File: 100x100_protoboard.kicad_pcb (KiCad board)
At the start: 2 copper layers, 97.8 x 96.5 mm, 418 parts, among them CON1 BARREL_JACK, CON2 USB_FEMALE_WITH_ID, CON3 USB_FEMALE_WITH_ID, J1 INTERCONNECT_1X03, J10 INTERCONNECT_1X03, J11 INTERCONNECT_1X03, J12 INTERCONNECT_1X03, J13 INTERCONNECT_1X03, J14 INTERCONNECT_1X03, J15 INTERCONNECT_1X03, J16 INTERCONNECT_1X03, J17 INTERCONNECT_1X03, J18 INTERCONNECT_1X03, J19 INTERCONNECT_1X03, J2 INTERCONNECT_1X03, J20 INTERCONNECT_1X03, J21 INTERCONNECT_1X03, J22 INTERCONNECT_1X03, J23 INTERCONNECT_1X03, J24 INTERCONNECT_1X03, J25 INTERCONNECT_1X03, J26 INTERCONNECT_1X03, J27 INTERCONNECT_1X03, J28 INTERCONNECT_1X03, J29 INTERCONNECT_1X03, J3 INTERCONNECT_1X03, J30 INTERCONNECT_1X03, J31 INTERCONNECT_1X03, J32 INTERCONNECT_1X03, J33 INTERCONNECT_1X03, J34 INTERCONNECT_1X03, J35 INTERCONNECT_1X03, J36 INTERCONNECT_1X03, J37 INTERCONNECT_1X03, J38 INTERCONNECT_1X03, J39 INTERCONNECT_1X03, J4 INTERCONNECT_1X03, J40 INTERCONNECT_1X03, J41 INTERCONNECT_1X03, J42 INTERCONNECT_1X03, J43 INTERCONNECT_1X03, J44 INTERCONNECT_1X03, J45 INTERCONNECT_1X03, J46 INTERCONNECT_1X03, J47 INTERCONNECT_1X03, J48 INTERCONNECT_1X03, J49 INTERCONNECT_1X03, J5 INTERCONNECT_1X03, J50 INTERCONNECT_1X03, J51 INTERCONNECT_1X03, J52 INTERCONNECT_1X03, J53 INTERCONNECT_1X03, J54 INTERCONNECT_1X03, J55 INTERCONNECT_1X03, J56 INTERCONNECT_1X03, J57 INTERCONNECT_1X03, J58 INTERCONNECT_1X03, J59 INTERCONNECT_1X03, J6 INTERCONNECT_1X03, J60 INTERCONNECT_1X03, J61 INTERCONNECT_1X03, J62 INTERCONNECT_1X03, J63 INTERCONNECT_1X03, J64 INTERCONNECT_1X03, J65 INTERCONNECT_1X02, J7 INTERCONNECT_1X03, J8 INTERCONNECT_1X03, J9 INTERCONNECT_1X03, P1 CONN_5, P1 CONN_8X2, P2 CONN_8X2, U1 LM7805CT

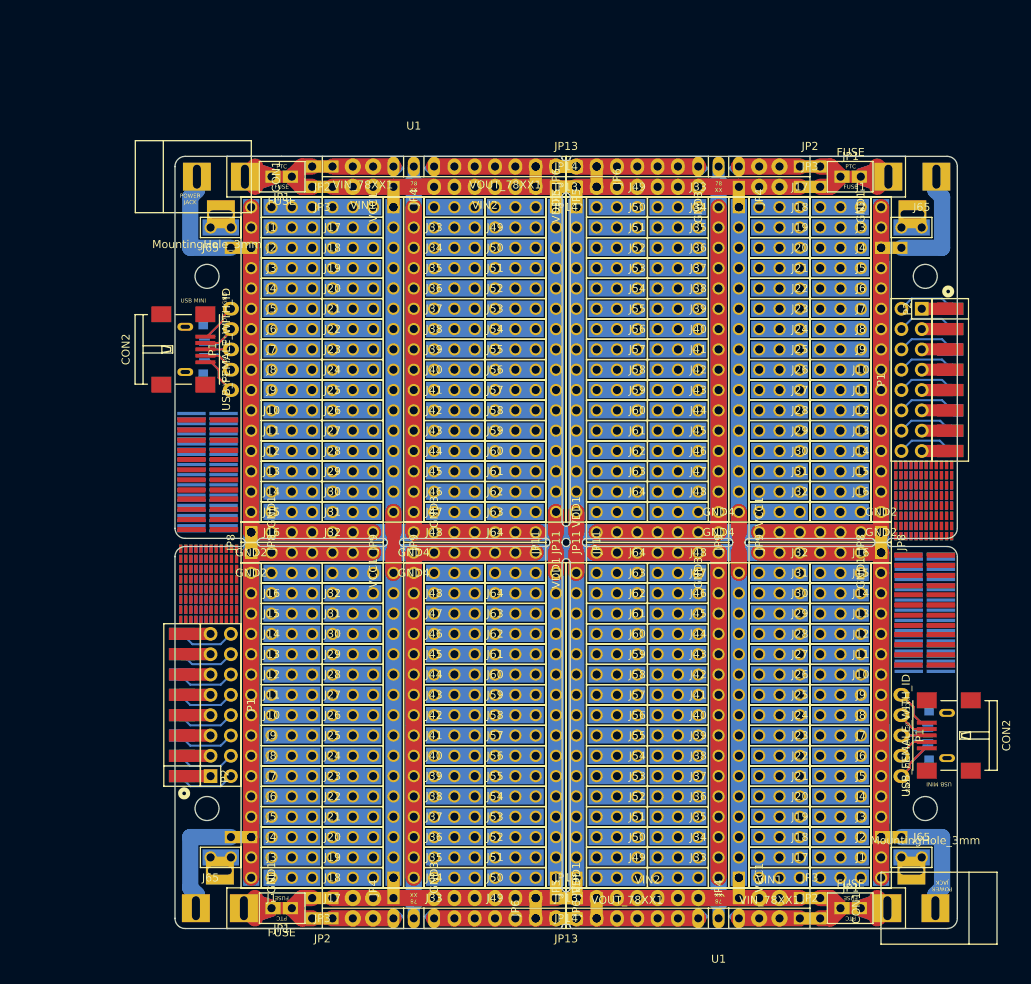
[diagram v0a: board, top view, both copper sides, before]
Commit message: added 3*3 mouse bites between the sub-boards on both edges
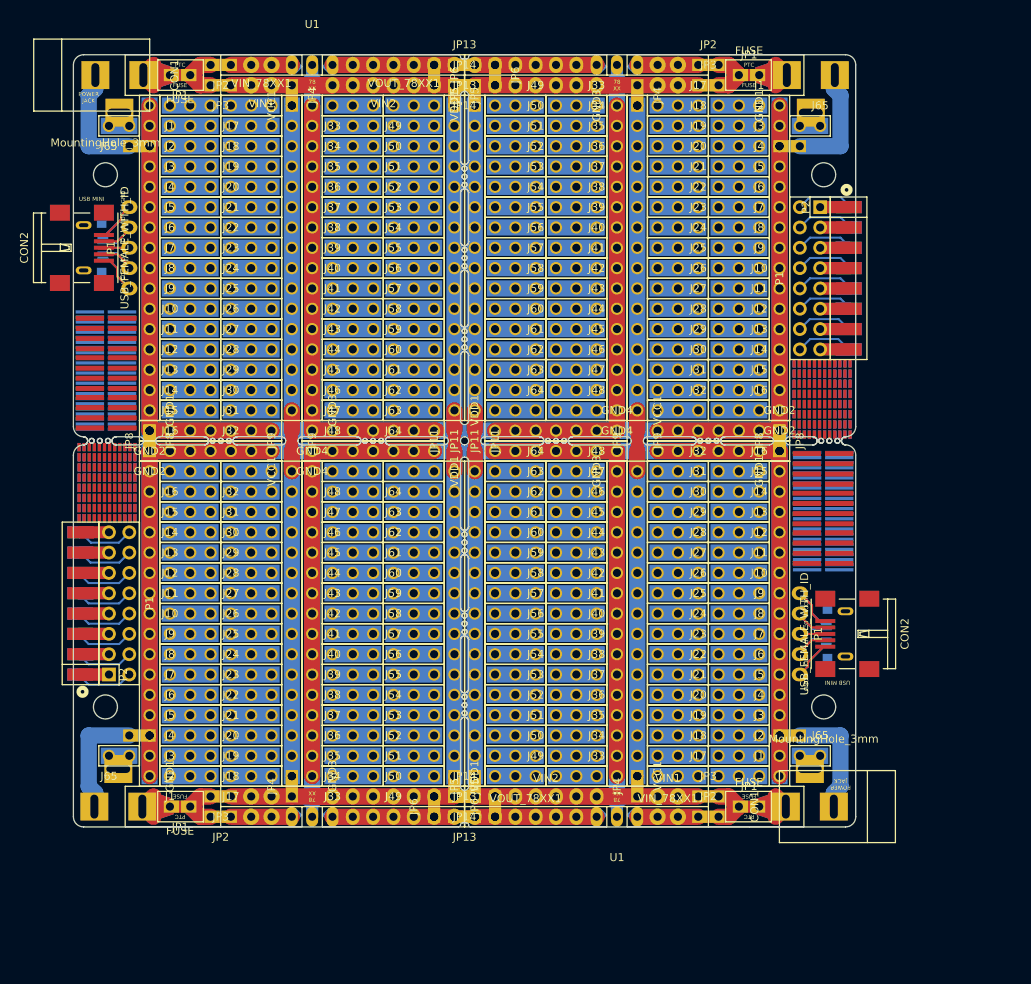
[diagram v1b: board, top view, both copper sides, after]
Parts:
- removed the C1 at (106.7, 35.3)
- removed the C1 at (106.7, 127.3)
- removed the C2 at (104.1, 35.3)
- removed the C2 at (104.1, 127.3)
- removed the CON1 at (132.8, 35.6)
- removed the CON1 at (132.7, 127.0)
- removed the F1 at (121.9, 35.6)
- removed the F1 at (121.9, 127.0)
- removed the F2 at (121.9, 35.6)
- removed the F2 at (121.9, 127.0)
- removed the GND1 at (125.7, 39.4)
- removed the GND1 at (125.7, 85.1)
- removed the GND2 at (125.7, 80.0)
- removed the GND2 at (125.7, 82.5)
- removed the GND3 at (105.4, 39.4)
- removed the GND3 at (105.4, 85.1)
- removed the GND4 at (105.4, 80.0)
- removed the GND4 at (105.4, 82.5)
- removed the J1 at (123.2, 39.4)
- removed the J1 at (123.2, 123.2)
- removed the J10 at (123.2, 62.2)
- removed the J10 at (123.2, 100.3)
- removed the J11 at (123.2, 64.8)
- removed the J11 at (123.2, 97.8)
- removed the J12 at (123.2, 67.3)
- removed the J12 at (123.2, 95.2)
- removed the J13 at (123.2, 69.8)
- removed the J13 at (123.2, 92.7)
- removed the J14 at (123.2, 72.4)
- removed the J14 at (123.2, 90.2)
- removed the J15 at (123.2, 74.9)
- removed the J15 at (123.2, 87.6)
- removed the J16 at (123.2, 77.5)
- removed the J16 at (123.2, 85.1)
- removed the J17 at (115.6, 39.4)
- removed the J17 at (115.6, 123.2)
- removed the J18 at (115.6, 41.9)
- removed the J18 at (115.6, 120.7)
- removed the J19 at (115.6, 44.5)
- removed the J19 at (115.6, 118.1)
- removed the J2 at (123.2, 41.9)
- removed the J2 at (123.2, 120.7)
- removed the J20 at (115.6, 47.0)
- removed the J20 at (115.6, 115.6)
- removed the J21 at (115.6, 49.5)
- removed the J21 at (115.6, 113.0)
- removed the J22 at (115.6, 52.1)
- removed the J22 at (115.6, 110.5)
- removed the J23 at (115.6, 54.6)
- removed the J23 at (115.6, 108.0)
- removed the J24 at (115.6, 57.1)
- removed the J24 at (115.6, 105.4)
- removed the J25 at (115.6, 59.7)
- removed the J25 at (115.6, 102.9)
- removed the J26 at (115.6, 62.2)
- removed the J26 at (115.6, 100.3)
- removed the J27 at (115.6, 64.8)
- removed the J27 at (115.6, 97.8)
- removed the J28 at (115.6, 67.3)
- removed the J28 at (115.6, 95.2)
- removed the J29 at (115.6, 69.8)
- removed the J29 at (115.6, 92.7)
- removed the J3 at (123.2, 44.5)
- removed the J3 at (123.2, 118.1)
- removed the J30 at (115.6, 72.4)
- removed the J30 at (115.6, 90.2)
- removed the J31 at (115.6, 74.9)
- removed the J31 at (115.6, 87.6)
- removed the J32 at (115.6, 77.5)
- removed the J32 at (115.6, 85.1)
- removed the J33 at (102.9, 39.4)
- removed the J33 at (102.9, 123.2)
- removed the J34 at (102.9, 41.9)
- removed the J34 at (102.9, 120.7)
- removed the J35 at (102.9, 44.5)
- removed the J35 at (102.9, 118.1)
- removed the J36 at (102.9, 47.0)
- removed the J36 at (102.9, 115.6)
- removed the J37 at (102.9, 49.5)
- removed the J37 at (102.9, 113.0)
- removed the J38 at (102.9, 52.1)
- removed the J38 at (102.9, 110.5)
- removed the J39 at (102.9, 54.6)
- removed the J39 at (102.9, 108.0)
- removed the J4 at (123.2, 47.0)
- removed the J4 at (123.2, 115.6)
- removed the J40 at (102.9, 57.1)
- removed the J40 at (102.9, 105.4)
- removed the J41 at (102.9, 59.7)
- removed the J41 at (102.9, 102.9)
- removed the J42 at (102.9, 62.2)
- removed the J42 at (102.9, 100.3)
- removed the J43 at (102.9, 64.8)
- removed the J43 at (102.9, 97.8)
- removed the J44 at (102.9, 67.3)
- removed the J44 at (102.9, 95.2)
- removed the J45 at (102.9, 69.8)
- removed the J45 at (102.9, 92.7)
- removed the J46 at (102.9, 72.4)
- removed the J46 at (102.9, 90.2)
- removed the J47 at (102.9, 74.9)
- removed the J47 at (102.9, 87.6)
- removed the J48 at (102.9, 77.5)
- removed the J48 at (102.9, 85.1)
- removed the J49 at (95.2, 39.4)
- removed the J49 at (95.2, 123.2)
- removed the J5 at (123.2, 49.5)
- removed the J5 at (123.2, 113.0)
- removed the J50 at (95.2, 41.9)
- removed the J50 at (95.2, 120.7)
- removed the J51 at (95.2, 44.5)
- removed the J51 at (95.2, 118.1)
- removed the J52 at (95.2, 47.0)
- removed the J52 at (95.2, 115.6)
- removed the J53 at (95.2, 49.5)
- removed the J53 at (95.2, 113.0)
- removed the J54 at (95.2, 52.1)
- removed the J54 at (95.2, 110.5)
- removed the J55 at (95.2, 54.6)
- removed the J55 at (95.2, 108.0)
- removed the J56 at (95.2, 57.1)
- removed the J56 at (95.2, 105.4)
- removed the J57 at (95.2, 59.7)
- removed the J57 at (95.2, 102.9)
- removed the J58 at (95.2, 62.2)
- removed the J58 at (95.2, 100.3)
- removed the J59 at (95.2, 64.8)
- removed the J59 at (95.2, 97.8)
- removed the J6 at (123.2, 52.1)
- removed the J6 at (123.2, 110.5)
- removed the J60 at (95.2, 67.3)
- removed the J60 at (95.2, 95.2)
- removed the J61 at (95.2, 69.8)
- removed the J61 at (95.2, 92.7)
- removed the J62 at (95.2, 72.4)
- removed the J62 at (95.2, 90.2)
- removed the J63 at (95.2, 74.9)
- removed the J63 at (95.2, 87.6)
- removed the J64 at (95.2, 77.5)
- removed the J64 at (95.2, 85.1)
- removed the J65 at (130.8, 41.9)
- removed the J65 at (130.8, 120.7)
- removed the J7 at (123.2, 54.6)
- removed the J7 at (123.2, 108.0)
- removed the J8 at (123.2, 57.1)
- removed the J8 at (123.2, 105.4)
- removed the J9 at (123.2, 59.7)
- removed the J9 at (123.2, 102.9)
- removed the JP1 at (121.9, 35.6)
- removed the JP1 at (121.9, 127.0)
- removed the JP10 at (87.6, 81.3) (x2)
- removed the JP11 at (87.6, 81.3) (x2)
- removed the JP12 at (86.4, 80.0)
- removed the JP12 at (86.4, 82.5)
- removed the JP13 at (86.4, 34.3)
- removed the JP13 at (86.4, 128.3)
- removed the JP14 at (86.4, 36.8)
- removed the JP14 at (86.4, 125.7)
- removed the JP15 at (108.0, 81.3) (x2)
- removed the JP2 at (116.8, 34.3)
- removed the JP2 at (116.8, 128.3)
- removed the JP3 at (116.8, 36.8)
- removed the JP3 at (116.8, 125.7)
- removed the JP4 at (108.0, 38.1)
- removed the JP4 at (108.0, 124.5)
- removed the JP5 at (87.6, 38.1)
- removed the JP5 at (87.6, 124.5)
- removed the JP6 at (90.2, 35.6)
- removed the JP6 at (90.2, 127.0)
- removed the JP7 at (127.0, 44.5)
- removed the JP7 at (127.0, 118.1)
- removed the JP8 at (125.7, 81.3) (x2)
- removed the JP9 at (108.0, 81.3) (x2)
- removed the MountingHole_3mm at (131.2, 48.0)
- removed the MountingHole_3mm at (131.2, 114.5)
- removed the P1 at (129.5, 61.0)
- removed the P1 at (128.3, 105.4)
- removed the Ref** at (131.7, 78.6) (x2)
- removed the Ref** at (131.2, 95.2)
- removed the Ref** at (131.7, 73.5) (x2)
- removed the Ref** at (131.2, 94.7)
- removed the Ref** at (131.2, 89.7)
- removed the Ref** at (131.2, 84.8)
- removed the Ref** at (131.2, 85.0)
- removed the Ref** at (131.2, 90.1)
- removed the U1 at (105.4, 34.3)
- removed the U1 at (105.4, 128.3)
- removed the VCC1 at (108.0, 77.5)
- removed the VCC1 at (108.0, 123.2)
- removed the VDD1 at (87.6, 39.4)
- removed the VDD1 at (87.6, 85.1)
- removed the VIN1 at (111.8, 36.8)
- removed the VIN1 at (111.8, 125.7)
- removed the VIN2 at (96.5, 36.8)
- removed the VIN2 at (96.5, 125.7)
- removed the VIN_78XX1 at (111.8, 34.3)
- removed the VIN_78XX1 at (111.8, 128.3)
- removed the VOUT_78XX1 at (94.0, 34.3)
- removed the VOUT_78XX1 at (94.0, 128.3)
- added C1: u33, Capacitors_SMD:C_0805_HandSoldering, B.Cu at (94.0, 22.6)
- added C1: u33, Capacitors_SMD:C_0805_HandSoldering, B.Cu at (94.0, 114.6)
- added C2: u1, Capacitors_SMD:C_0805_HandSoldering, B.Cu at (91.4, 22.6)
- added C2: u1, Capacitors_SMD:C_0805_HandSoldering, B.Cu at (91.4, 114.6)
- added CON1: BARREL_JACK, Connect:BARREL_JACK, B.Cu at (120.1, 22.9)
- added CON1: BARREL_JACK, Connect:BARREL_JACK, F.Cu at (120.0, 114.3)
- added F1: FUSE, Muonde:CC12ZZ, B.Cu at (109.2, 22.9)
- added F1: FUSE, Muonde:CC12ZZ, F.Cu at (109.2, 114.3)
- added F2: FUSE, Muonde:CC12ZZ, F.Cu at (109.2, 22.9)
- added F2: FUSE, Muonde:CC12ZZ, B.Cu at (109.2, 114.3)
- added GND1: INTERCONNECT_1X16, 2.54mm_Pin_Headers:Interconnect_1x16, F.Cu at (113.0, 26.7)
- added GND1: INTERCONNECT_1X16, 2.54mm_Pin_Headers:Interconnect_1x16, F.Cu at (113.0, 72.4)
- added GND2: INTERCONNECT_1X07, 2.54mm_Pin_Headers:Interconnect_1x07, F.Cu at (113.0, 67.3)
- added GND2: INTERCONNECT_1X07, 2.54mm_Pin_Headers:Interconnect_1x07, F.Cu at (113.0, 69.8)
- added GND3: INTERCONNECT_1X16, 2.54mm_Pin_Headers:Interconnect_1x16, F.Cu at (92.7, 26.7)
- added GND3: INTERCONNECT_1X16, 2.54mm_Pin_Headers:Interconnect_1x16, F.Cu at (92.7, 72.4)
- added GND4: INTERCONNECT_1X07, 2.54mm_Pin_Headers:Interconnect_1x07, F.Cu at (92.7, 67.3)
- added GND4: INTERCONNECT_1X07, 2.54mm_Pin_Headers:Interconnect_1x07, F.Cu at (92.7, 69.8)
- added J1: INTERCONNECT_1X03, 2.54mm_Pin_Headers:Interconnect_1x03, F.Cu at (110.5, 26.7)
- added J1: INTERCONNECT_1X03, 2.54mm_Pin_Headers:Interconnect_1x03, F.Cu at (110.5, 110.5)
- added J10: INTERCONNECT_1X03, 2.54mm_Pin_Headers:Interconnect_1x03, F.Cu at (110.5, 49.5)
- added J10: INTERCONNECT_1X03, 2.54mm_Pin_Headers:Interconnect_1x03, F.Cu at (110.5, 87.6)
- added J11: INTERCONNECT_1X03, 2.54mm_Pin_Headers:Interconnect_1x03, F.Cu at (110.5, 52.1)
- added J11: INTERCONNECT_1X03, 2.54mm_Pin_Headers:Interconnect_1x03, F.Cu at (110.5, 85.1)
- added J12: INTERCONNECT_1X03, 2.54mm_Pin_Headers:Interconnect_1x03, F.Cu at (110.5, 54.6)
- added J12: INTERCONNECT_1X03, 2.54mm_Pin_Headers:Interconnect_1x03, F.Cu at (110.5, 82.5)
- added J13: INTERCONNECT_1X03, 2.54mm_Pin_Headers:Interconnect_1x03, F.Cu at (110.5, 57.1)
- added J13: INTERCONNECT_1X03, 2.54mm_Pin_Headers:Interconnect_1x03, F.Cu at (110.5, 80.0)
- added J14: INTERCONNECT_1X03, 2.54mm_Pin_Headers:Interconnect_1x03, F.Cu at (110.5, 59.7)
- added J14: INTERCONNECT_1X03, 2.54mm_Pin_Headers:Interconnect_1x03, F.Cu at (110.5, 77.5)
- added J15: INTERCONNECT_1X03, 2.54mm_Pin_Headers:Interconnect_1x03, F.Cu at (110.5, 62.2)
- added J15: INTERCONNECT_1X03, 2.54mm_Pin_Headers:Interconnect_1x03, F.Cu at (110.5, 74.9)
- added J16: INTERCONNECT_1X03, 2.54mm_Pin_Headers:Interconnect_1x03, F.Cu at (110.5, 64.8)
- added J16: INTERCONNECT_1X03, 2.54mm_Pin_Headers:Interconnect_1x03, F.Cu at (110.5, 72.4)
- added J17: INTERCONNECT_1X03, 2.54mm_Pin_Headers:Interconnect_1x03, F.Cu at (102.9, 26.7)
- added J17: INTERCONNECT_1X03, 2.54mm_Pin_Headers:Interconnect_1x03, F.Cu at (102.9, 110.5)
- added J18: INTERCONNECT_1X03, 2.54mm_Pin_Headers:Interconnect_1x03, F.Cu at (102.9, 29.2)
- added J18: INTERCONNECT_1X03, 2.54mm_Pin_Headers:Interconnect_1x03, F.Cu at (102.9, 108.0)
- added J19: INTERCONNECT_1X03, 2.54mm_Pin_Headers:Interconnect_1x03, F.Cu at (102.9, 31.8)
- added J19: INTERCONNECT_1X03, 2.54mm_Pin_Headers:Interconnect_1x03, F.Cu at (102.9, 105.4)
- added J2: INTERCONNECT_1X03, 2.54mm_Pin_Headers:Interconnect_1x03, F.Cu at (110.5, 29.2)
- added J2: INTERCONNECT_1X03, 2.54mm_Pin_Headers:Interconnect_1x03, F.Cu at (110.5, 108.0)
- added J20: INTERCONNECT_1X03, 2.54mm_Pin_Headers:Interconnect_1x03, F.Cu at (102.9, 34.3)
- added J20: INTERCONNECT_1X03, 2.54mm_Pin_Headers:Interconnect_1x03, F.Cu at (102.9, 102.9)
- added J21: INTERCONNECT_1X03, 2.54mm_Pin_Headers:Interconnect_1x03, F.Cu at (102.9, 36.8)
- added J21: INTERCONNECT_1X03, 2.54mm_Pin_Headers:Interconnect_1x03, F.Cu at (102.9, 100.3)
- added J22: INTERCONNECT_1X03, 2.54mm_Pin_Headers:Interconnect_1x03, F.Cu at (102.9, 39.4)
- added J22: INTERCONNECT_1X03, 2.54mm_Pin_Headers:Interconnect_1x03, F.Cu at (102.9, 97.8)
- added J23: INTERCONNECT_1X03, 2.54mm_Pin_Headers:Interconnect_1x03, F.Cu at (102.9, 41.9)
- added J23: INTERCONNECT_1X03, 2.54mm_Pin_Headers:Interconnect_1x03, F.Cu at (102.9, 95.2)
- added J24: INTERCONNECT_1X03, 2.54mm_Pin_Headers:Interconnect_1x03, F.Cu at (102.9, 44.5)
- added J24: INTERCONNECT_1X03, 2.54mm_Pin_Headers:Interconnect_1x03, F.Cu at (102.9, 92.7)
- added J25: INTERCONNECT_1X03, 2.54mm_Pin_Headers:Interconnect_1x03, F.Cu at (102.9, 47.0)
- added J25: INTERCONNECT_1X03, 2.54mm_Pin_Headers:Interconnect_1x03, F.Cu at (102.9, 90.2)
- added J26: INTERCONNECT_1X03, 2.54mm_Pin_Headers:Interconnect_1x03, F.Cu at (102.9, 49.5)
- added J26: INTERCONNECT_1X03, 2.54mm_Pin_Headers:Interconnect_1x03, F.Cu at (102.9, 87.6)
- added J27: INTERCONNECT_1X03, 2.54mm_Pin_Headers:Interconnect_1x03, F.Cu at (102.9, 52.1)
- added J27: INTERCONNECT_1X03, 2.54mm_Pin_Headers:Interconnect_1x03, F.Cu at (102.9, 85.1)
- added J28: INTERCONNECT_1X03, 2.54mm_Pin_Headers:Interconnect_1x03, F.Cu at (102.9, 54.6)
- added J28: INTERCONNECT_1X03, 2.54mm_Pin_Headers:Interconnect_1x03, F.Cu at (102.9, 82.5)
- added J29: INTERCONNECT_1X03, 2.54mm_Pin_Headers:Interconnect_1x03, F.Cu at (102.9, 57.1)
- added J29: INTERCONNECT_1X03, 2.54mm_Pin_Headers:Interconnect_1x03, F.Cu at (102.9, 80.0)
- added J3: INTERCONNECT_1X03, 2.54mm_Pin_Headers:Interconnect_1x03, F.Cu at (110.5, 31.8)
- added J3: INTERCONNECT_1X03, 2.54mm_Pin_Headers:Interconnect_1x03, F.Cu at (110.5, 105.4)
- added J30: INTERCONNECT_1X03, 2.54mm_Pin_Headers:Interconnect_1x03, F.Cu at (102.9, 59.7)
- added J30: INTERCONNECT_1X03, 2.54mm_Pin_Headers:Interconnect_1x03, F.Cu at (102.9, 77.5)
- added J31: INTERCONNECT_1X03, 2.54mm_Pin_Headers:Interconnect_1x03, F.Cu at (102.9, 62.2)
- added J31: INTERCONNECT_1X03, 2.54mm_Pin_Headers:Interconnect_1x03, F.Cu at (102.9, 74.9)
- added J32: INTERCONNECT_1X03, 2.54mm_Pin_Headers:Interconnect_1x03, F.Cu at (102.9, 64.8)
- added J32: INTERCONNECT_1X03, 2.54mm_Pin_Headers:Interconnect_1x03, F.Cu at (102.9, 72.4)
- added J33: INTERCONNECT_1X03, 2.54mm_Pin_Headers:Interconnect_1x03, F.Cu at (90.2, 26.7)
- added J33: INTERCONNECT_1X03, 2.54mm_Pin_Headers:Interconnect_1x03, F.Cu at (90.2, 110.5)
- added J34: INTERCONNECT_1X03, 2.54mm_Pin_Headers:Interconnect_1x03, F.Cu at (90.2, 29.2)
- added J34: INTERCONNECT_1X03, 2.54mm_Pin_Headers:Interconnect_1x03, F.Cu at (90.2, 108.0)
- added J35: INTERCONNECT_1X03, 2.54mm_Pin_Headers:Interconnect_1x03, F.Cu at (90.2, 31.8)
- added J35: INTERCONNECT_1X03, 2.54mm_Pin_Headers:Interconnect_1x03, F.Cu at (90.2, 105.4)
- added J36: INTERCONNECT_1X03, 2.54mm_Pin_Headers:Interconnect_1x03, F.Cu at (90.2, 34.3)
- added J36: INTERCONNECT_1X03, 2.54mm_Pin_Headers:Interconnect_1x03, F.Cu at (90.2, 102.9)
- added J37: INTERCONNECT_1X03, 2.54mm_Pin_Headers:Interconnect_1x03, F.Cu at (90.2, 36.8)
- added J37: INTERCONNECT_1X03, 2.54mm_Pin_Headers:Interconnect_1x03, F.Cu at (90.2, 100.3)
- added J38: INTERCONNECT_1X03, 2.54mm_Pin_Headers:Interconnect_1x03, F.Cu at (90.2, 39.4)
- added J38: INTERCONNECT_1X03, 2.54mm_Pin_Headers:Interconnect_1x03, F.Cu at (90.2, 97.8)
- added J39: INTERCONNECT_1X03, 2.54mm_Pin_Headers:Interconnect_1x03, F.Cu at (90.2, 41.9)
- added J39: INTERCONNECT_1X03, 2.54mm_Pin_Headers:Interconnect_1x03, F.Cu at (90.2, 95.2)
- added J4: INTERCONNECT_1X03, 2.54mm_Pin_Headers:Interconnect_1x03, F.Cu at (110.5, 34.3)
- added J4: INTERCONNECT_1X03, 2.54mm_Pin_Headers:Interconnect_1x03, F.Cu at (110.5, 102.9)
- added J40: INTERCONNECT_1X03, 2.54mm_Pin_Headers:Interconnect_1x03, F.Cu at (90.2, 44.5)
- added J40: INTERCONNECT_1X03, 2.54mm_Pin_Headers:Interconnect_1x03, F.Cu at (90.2, 92.7)
- added J41: INTERCONNECT_1X03, 2.54mm_Pin_Headers:Interconnect_1x03, F.Cu at (90.2, 47.0)
- added J41: INTERCONNECT_1X03, 2.54mm_Pin_Headers:Interconnect_1x03, F.Cu at (90.2, 90.2)
- added J42: INTERCONNECT_1X03, 2.54mm_Pin_Headers:Interconnect_1x03, F.Cu at (90.2, 49.5)
- added J42: INTERCONNECT_1X03, 2.54mm_Pin_Headers:Interconnect_1x03, F.Cu at (90.2, 87.6)
- added J43: INTERCONNECT_1X03, 2.54mm_Pin_Headers:Interconnect_1x03, F.Cu at (90.2, 52.1)
- added J43: INTERCONNECT_1X03, 2.54mm_Pin_Headers:Interconnect_1x03, F.Cu at (90.2, 85.1)
- added J44: INTERCONNECT_1X03, 2.54mm_Pin_Headers:Interconnect_1x03, F.Cu at (90.2, 54.6)
- added J44: INTERCONNECT_1X03, 2.54mm_Pin_Headers:Interconnect_1x03, F.Cu at (90.2, 82.5)
- added J45: INTERCONNECT_1X03, 2.54mm_Pin_Headers:Interconnect_1x03, F.Cu at (90.2, 57.1)
- added J45: INTERCONNECT_1X03, 2.54mm_Pin_Headers:Interconnect_1x03, F.Cu at (90.2, 80.0)
- added J46: INTERCONNECT_1X03, 2.54mm_Pin_Headers:Interconnect_1x03, F.Cu at (90.2, 59.7)
- added J46: INTERCONNECT_1X03, 2.54mm_Pin_Headers:Interconnect_1x03, F.Cu at (90.2, 77.5)
- added J47: INTERCONNECT_1X03, 2.54mm_Pin_Headers:Interconnect_1x03, F.Cu at (90.2, 62.2)
- added J47: INTERCONNECT_1X03, 2.54mm_Pin_Headers:Interconnect_1x03, F.Cu at (90.2, 74.9)
- added J48: INTERCONNECT_1X03, 2.54mm_Pin_Headers:Interconnect_1x03, F.Cu at (90.2, 64.8)
- added J48: INTERCONNECT_1X03, 2.54mm_Pin_Headers:Interconnect_1x03, F.Cu at (90.2, 72.4)
- added J49: INTERCONNECT_1X03, 2.54mm_Pin_Headers:Interconnect_1x03, F.Cu at (82.5, 26.7)
- added J49: INTERCONNECT_1X03, 2.54mm_Pin_Headers:Interconnect_1x03, F.Cu at (82.5, 110.5)
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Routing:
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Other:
- outline, holes or cut-outs redrawn

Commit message: Revert "added 3*3 mouse bites between the sub-boards on both edges"
This reverts commit 72bb31031476af87d888838294cc72f0395ed406.

it turns out that mouse bites shorts the rails if the board house does
not adhere to the NPTH drill directions, which kind of makes up for the
usefulness that the mouse bites provided. and they did not improve the
board sturdiness significantly, so it is not a problem to remove them.
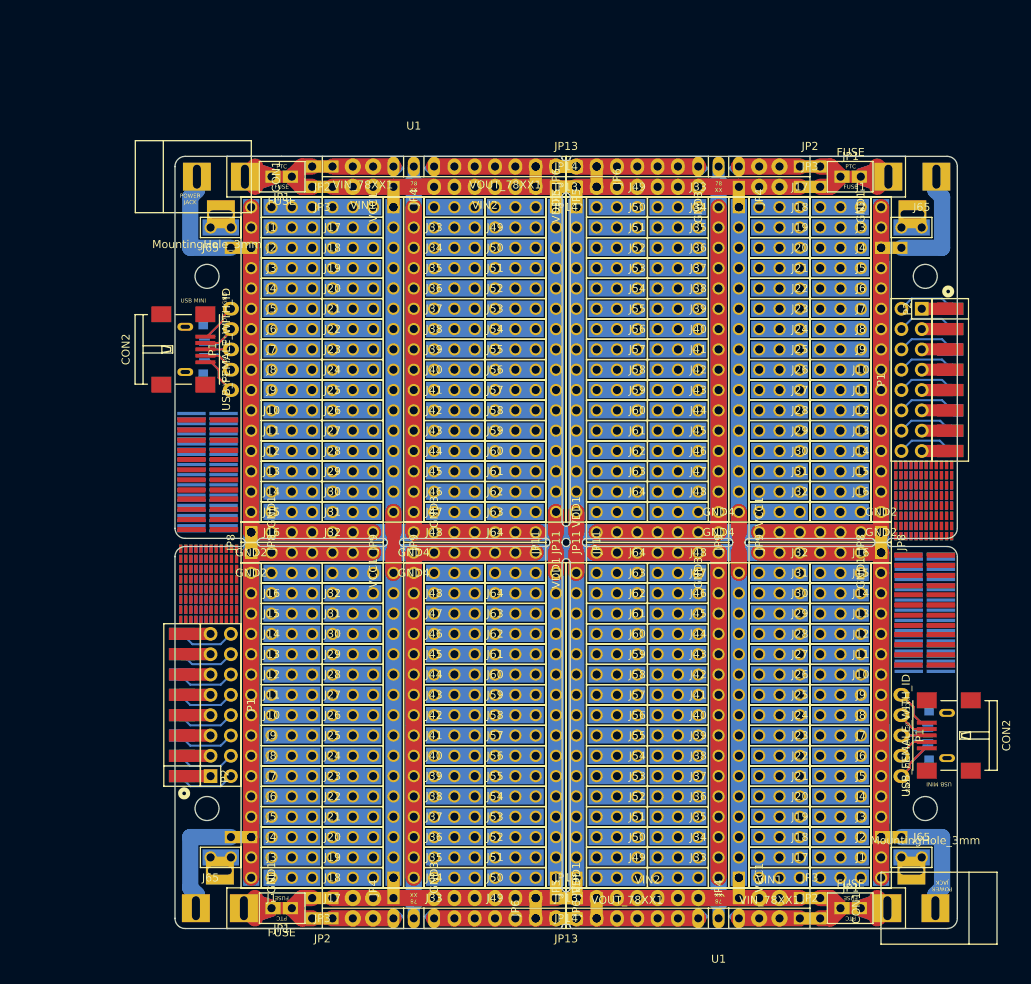
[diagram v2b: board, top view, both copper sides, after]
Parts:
- removed the C1 at (94.0, 22.6)
- removed the C1 at (94.0, 114.6)
- removed the C2 at (91.4, 22.6)
- removed the C2 at (91.4, 114.6)
- removed the CON1 at (120.1, 22.9)
- removed the CON1 at (120.0, 114.3)
- removed the F1 at (109.2, 22.9)
- removed the F1 at (109.2, 114.3)
- removed the F2 at (109.2, 22.9)
- removed the F2 at (109.2, 114.3)
- removed the GND1 at (113.0, 26.7)
- removed the GND1 at (113.0, 72.4)
- removed the GND2 at (113.0, 67.3)
- removed the GND2 at (113.0, 69.8)
- removed the GND3 at (92.7, 26.7)
- removed the GND3 at (92.7, 72.4)
- removed the GND4 at (92.7, 67.3)
- removed the GND4 at (92.7, 69.8)
- removed the J1 at (110.5, 26.7)
- removed the J1 at (110.5, 110.5)
- removed the J10 at (110.5, 49.5)
- removed the J10 at (110.5, 87.6)
- removed the J11 at (110.5, 52.1)
- removed the J11 at (110.5, 85.1)
- removed the J12 at (110.5, 54.6)
- removed the J12 at (110.5, 82.5)
- removed the J13 at (110.5, 57.1)
- removed the J13 at (110.5, 80.0)
- removed the J14 at (110.5, 59.7)
- removed the J14 at (110.5, 77.5)
- removed the J15 at (110.5, 62.2)
- removed the J15 at (110.5, 74.9)
- removed the J16 at (110.5, 64.8)
- removed the J16 at (110.5, 72.4)
- removed the J17 at (102.9, 26.7)
- removed the J17 at (102.9, 110.5)
- removed the J18 at (102.9, 29.2)
- removed the J18 at (102.9, 108.0)
- removed the J19 at (102.9, 31.8)
- removed the J19 at (102.9, 105.4)
- removed the J2 at (110.5, 29.2)
- removed the J2 at (110.5, 108.0)
- removed the J20 at (102.9, 34.3)
- removed the J20 at (102.9, 102.9)
- removed the J21 at (102.9, 36.8)
- removed the J21 at (102.9, 100.3)
- removed the J22 at (102.9, 39.4)
- removed the J22 at (102.9, 97.8)
- removed the J23 at (102.9, 41.9)
- removed the J23 at (102.9, 95.2)
- removed the J24 at (102.9, 44.5)
- removed the J24 at (102.9, 92.7)
- removed the J25 at (102.9, 47.0)
- removed the J25 at (102.9, 90.2)
- removed the J26 at (102.9, 49.5)
- removed the J26 at (102.9, 87.6)
- removed the J27 at (102.9, 52.1)
- removed the J27 at (102.9, 85.1)
- removed the J28 at (102.9, 54.6)
- removed the J28 at (102.9, 82.5)
- removed the J29 at (102.9, 57.1)
- removed the J29 at (102.9, 80.0)
- removed the J3 at (110.5, 31.8)
- removed the J3 at (110.5, 105.4)
- removed the J30 at (102.9, 59.7)
- removed the J30 at (102.9, 77.5)
- removed the J31 at (102.9, 62.2)
- removed the J31 at (102.9, 74.9)
- removed the J32 at (102.9, 64.8)
- removed the J32 at (102.9, 72.4)
- removed the J33 at (90.2, 26.7)
- removed the J33 at (90.2, 110.5)
- removed the J34 at (90.2, 29.2)
- removed the J34 at (90.2, 108.0)
- removed the J35 at (90.2, 31.8)
- removed the J35 at (90.2, 105.4)
- removed the J36 at (90.2, 34.3)
- removed the J36 at (90.2, 102.9)
- removed the J37 at (90.2, 36.8)
- removed the J37 at (90.2, 100.3)
- removed the J38 at (90.2, 39.4)
- removed the J38 at (90.2, 97.8)
- removed the J39 at (90.2, 41.9)
- removed the J39 at (90.2, 95.2)
- removed the J4 at (110.5, 34.3)
- removed the J4 at (110.5, 102.9)
- removed the J40 at (90.2, 44.5)
- removed the J40 at (90.2, 92.7)
- removed the J41 at (90.2, 47.0)
- removed the J41 at (90.2, 90.2)
- removed the J42 at (90.2, 49.5)
- removed the J42 at (90.2, 87.6)
- removed the J43 at (90.2, 52.1)
- removed the J43 at (90.2, 85.1)
- removed the J44 at (90.2, 54.6)
- removed the J44 at (90.2, 82.5)
- removed the J45 at (90.2, 57.1)
- removed the J45 at (90.2, 80.0)
- removed the J46 at (90.2, 59.7)
- removed the J46 at (90.2, 77.5)
- removed the J47 at (90.2, 62.2)
- removed the J47 at (90.2, 74.9)
- removed the J48 at (90.2, 64.8)
- removed the J48 at (90.2, 72.4)
- removed the J49 at (82.5, 26.7)
- removed the J49 at (82.5, 110.5)
- removed the J5 at (110.5, 36.8)
- removed the J5 at (110.5, 100.3)
- removed the J50 at (82.5, 29.2)
- removed the J50 at (82.5, 108.0)
- removed the J51 at (82.5, 31.8)
- removed the J51 at (82.5, 105.4)
- removed the J52 at (82.5, 34.3)
- removed the J52 at (82.5, 102.9)
- removed the J53 at (82.5, 36.8)
- removed the J53 at (82.5, 100.3)
- removed the J54 at (82.5, 39.4)
- removed the J54 at (82.5, 97.8)
- removed the J55 at (82.5, 41.9)
- removed the J55 at (82.5, 95.2)
- removed the J56 at (82.5, 44.5)
- removed the J56 at (82.5, 92.7)
- removed the J57 at (82.5, 47.0)
- removed the J57 at (82.5, 90.2)
- removed the J58 at (82.5, 49.5)
- removed the J58 at (82.5, 87.6)
- removed the J59 at (82.5, 52.1)
- removed the J59 at (82.5, 85.1)
- removed the J6 at (110.5, 39.4)
- removed the J6 at (110.5, 97.8)
- removed the J60 at (82.5, 54.6)
- removed the J60 at (82.5, 82.5)
- removed the J61 at (82.5, 57.1)
- removed the J61 at (82.5, 80.0)
- removed the J62 at (82.5, 59.7)
- removed the J62 at (82.5, 77.5)
- removed the J63 at (82.5, 62.2)
- removed the J63 at (82.5, 74.9)
- removed the J64 at (82.5, 64.8)
- removed the J64 at (82.5, 72.4)
- removed the J65 at (118.1, 29.2)
- removed the J65 at (118.1, 108.0)
- removed the J7 at (110.5, 41.9)
- removed the J7 at (110.5, 95.2)
- removed the J8 at (110.5, 44.5)
- removed the J8 at (110.5, 92.7)
- removed the J9 at (110.5, 47.0)
- removed the J9 at (110.5, 90.2)
- removed the JP1 at (109.2, 22.9)
- removed the JP1 at (109.2, 114.3)
- removed the JP10 at (74.9, 68.6) (x2)
- removed the JP11 at (74.9, 68.6) (x2)
- removed the JP12 at (73.7, 67.3)
- removed the JP12 at (73.7, 69.8)
- removed the JP13 at (73.7, 21.6)
- removed the JP13 at (73.7, 115.6)
- removed the JP14 at (73.7, 24.1)
- removed the JP14 at (73.7, 113.0)
- removed the JP15 at (95.2, 68.6) (x2)
- removed the JP2 at (104.1, 21.6)
- removed the JP2 at (104.1, 115.6)
- removed the JP3 at (104.1, 24.1)
- removed the JP3 at (104.1, 113.0)
- removed the JP4 at (95.2, 25.4)
- removed the JP4 at (95.2, 111.8)
- removed the JP5 at (74.9, 25.4)
- removed the JP5 at (74.9, 111.8)
- removed the JP6 at (77.5, 22.9)
- removed the JP6 at (77.5, 114.3)
- removed the JP7 at (114.3, 31.8)
- removed the JP7 at (114.3, 105.4)
- removed the JP8 at (113.0, 68.6) (x2)
- removed the JP9 at (95.2, 68.6) (x2)
- removed the MountingHole_3mm at (118.5, 35.3)
- removed the MountingHole_3mm at (118.5, 101.8)
- removed Mouse_Bites_3_1.27mm (x24): VAL**, Misc:Mouse_Bites_3_1.016mm
- removed the P1 at (116.8, 48.3)
- removed the P1 at (115.6, 92.7)
- removed the Ref** at (119.0, 65.9) (x2)
- removed the Ref** at (118.5, 82.5)
- removed the Ref** at (119.0, 60.8) (x2)
- removed the Ref** at (118.5, 82.0)
- removed the Ref** at (118.5, 77.0)
- removed the Ref** at (118.5, 72.1)
- removed the Ref** at (118.5, 72.3)
- removed the Ref** at (118.5, 77.4)
- removed the U1 at (92.7, 21.6)
- removed the U1 at (92.7, 115.6)
- removed the VCC1 at (95.2, 64.8)
- removed the VCC1 at (95.2, 110.5)
- removed the VDD1 at (74.9, 26.7)
- removed the VDD1 at (74.9, 72.4)
- removed the VIN1 at (99.1, 24.1)
- removed the VIN1 at (99.1, 113.0)
- removed the VIN2 at (83.8, 24.1)
- removed the VIN2 at (83.8, 113.0)
- removed the VIN_78XX1 at (99.1, 21.6)
- removed the VIN_78XX1 at (99.1, 115.6)
- removed the VOUT_78XX1 at (81.3, 21.6)
- removed the VOUT_78XX1 at (81.3, 115.6)
- added C1: u33, Capacitors_SMD:C_0805_HandSoldering, B.Cu at (106.7, 35.3)
- added C1: u33, Capacitors_SMD:C_0805_HandSoldering, B.Cu at (106.7, 127.3)
- added C2: u1, Capacitors_SMD:C_0805_HandSoldering, B.Cu at (104.1, 35.3)
- added C2: u1, Capacitors_SMD:C_0805_HandSoldering, B.Cu at (104.1, 127.3)
- added CON1: BARREL_JACK, Connect:BARREL_JACK, B.Cu at (132.8, 35.6)
- added CON1: BARREL_JACK, Connect:BARREL_JACK, F.Cu at (132.7, 127.0)
- added F1: FUSE, Muonde:CC12ZZ, B.Cu at (121.9, 35.6)
- added F1: FUSE, Muonde:CC12ZZ, F.Cu at (121.9, 127.0)
- added F2: FUSE, Muonde:CC12ZZ, F.Cu at (121.9, 35.6)
- added F2: FUSE, Muonde:CC12ZZ, B.Cu at (121.9, 127.0)
- added GND1: INTERCONNECT_1X16, 2.54mm_Pin_Headers:Interconnect_1x16, F.Cu at (125.7, 39.4)
- added GND1: INTERCONNECT_1X16, 2.54mm_Pin_Headers:Interconnect_1x16, F.Cu at (125.7, 85.1)
- added GND2: INTERCONNECT_1X07, 2.54mm_Pin_Headers:Interconnect_1x07, F.Cu at (125.7, 80.0)
- added GND2: INTERCONNECT_1X07, 2.54mm_Pin_Headers:Interconnect_1x07, F.Cu at (125.7, 82.5)
- added GND3: INTERCONNECT_1X16, 2.54mm_Pin_Headers:Interconnect_1x16, F.Cu at (105.4, 39.4)
- added GND3: INTERCONNECT_1X16, 2.54mm_Pin_Headers:Interconnect_1x16, F.Cu at (105.4, 85.1)
- added GND4: INTERCONNECT_1X07, 2.54mm_Pin_Headers:Interconnect_1x07, F.Cu at (105.4, 80.0)
- added GND4: INTERCONNECT_1X07, 2.54mm_Pin_Headers:Interconnect_1x07, F.Cu at (105.4, 82.5)
- added J1: INTERCONNECT_1X03, 2.54mm_Pin_Headers:Interconnect_1x03, F.Cu at (123.2, 39.4)
- added J1: INTERCONNECT_1X03, 2.54mm_Pin_Headers:Interconnect_1x03, F.Cu at (123.2, 123.2)
- added J10: INTERCONNECT_1X03, 2.54mm_Pin_Headers:Interconnect_1x03, F.Cu at (123.2, 62.2)
- added J10: INTERCONNECT_1X03, 2.54mm_Pin_Headers:Interconnect_1x03, F.Cu at (123.2, 100.3)
- added J11: INTERCONNECT_1X03, 2.54mm_Pin_Headers:Interconnect_1x03, F.Cu at (123.2, 64.8)
- added J11: INTERCONNECT_1X03, 2.54mm_Pin_Headers:Interconnect_1x03, F.Cu at (123.2, 97.8)
- added J12: INTERCONNECT_1X03, 2.54mm_Pin_Headers:Interconnect_1x03, F.Cu at (123.2, 67.3)
- added J12: INTERCONNECT_1X03, 2.54mm_Pin_Headers:Interconnect_1x03, F.Cu at (123.2, 95.2)
- added J13: INTERCONNECT_1X03, 2.54mm_Pin_Headers:Interconnect_1x03, F.Cu at (123.2, 69.8)
- added J13: INTERCONNECT_1X03, 2.54mm_Pin_Headers:Interconnect_1x03, F.Cu at (123.2, 92.7)
- added J14: INTERCONNECT_1X03, 2.54mm_Pin_Headers:Interconnect_1x03, F.Cu at (123.2, 72.4)
- added J14: INTERCONNECT_1X03, 2.54mm_Pin_Headers:Interconnect_1x03, F.Cu at (123.2, 90.2)
- added J15: INTERCONNECT_1X03, 2.54mm_Pin_Headers:Interconnect_1x03, F.Cu at (123.2, 74.9)
- added J15: INTERCONNECT_1X03, 2.54mm_Pin_Headers:Interconnect_1x03, F.Cu at (123.2, 87.6)
- added J16: INTERCONNECT_1X03, 2.54mm_Pin_Headers:Interconnect_1x03, F.Cu at (123.2, 77.5)
- added J16: INTERCONNECT_1X03, 2.54mm_Pin_Headers:Interconnect_1x03, F.Cu at (123.2, 85.1)
- added J17: INTERCONNECT_1X03, 2.54mm_Pin_Headers:Interconnect_1x03, F.Cu at (115.6, 39.4)
- added J17: INTERCONNECT_1X03, 2.54mm_Pin_Headers:Interconnect_1x03, F.Cu at (115.6, 123.2)
- added J18: INTERCONNECT_1X03, 2.54mm_Pin_Headers:Interconnect_1x03, F.Cu at (115.6, 41.9)
- added J18: INTERCONNECT_1X03, 2.54mm_Pin_Headers:Interconnect_1x03, F.Cu at (115.6, 120.7)
- added J19: INTERCONNECT_1X03, 2.54mm_Pin_Headers:Interconnect_1x03, F.Cu at (115.6, 44.5)
- added J19: INTERCONNECT_1X03, 2.54mm_Pin_Headers:Interconnect_1x03, F.Cu at (115.6, 118.1)
- added J2: INTERCONNECT_1X03, 2.54mm_Pin_Headers:Interconnect_1x03, F.Cu at (123.2, 41.9)
- added J2: INTERCONNECT_1X03, 2.54mm_Pin_Headers:Interconnect_1x03, F.Cu at (123.2, 120.7)
- added J20: INTERCONNECT_1X03, 2.54mm_Pin_Headers:Interconnect_1x03, F.Cu at (115.6, 47.0)
- added J20: INTERCONNECT_1X03, 2.54mm_Pin_Headers:Interconnect_1x03, F.Cu at (115.6, 115.6)
- added J21: INTERCONNECT_1X03, 2.54mm_Pin_Headers:Interconnect_1x03, F.Cu at (115.6, 49.5)
- added J21: INTERCONNECT_1X03, 2.54mm_Pin_Headers:Interconnect_1x03, F.Cu at (115.6, 113.0)
- added J22: INTERCONNECT_1X03, 2.54mm_Pin_Headers:Interconnect_1x03, F.Cu at (115.6, 52.1)
- added J22: INTERCONNECT_1X03, 2.54mm_Pin_Headers:Interconnect_1x03, F.Cu at (115.6, 110.5)
- added J23: INTERCONNECT_1X03, 2.54mm_Pin_Headers:Interconnect_1x03, F.Cu at (115.6, 54.6)
- added J23: INTERCONNECT_1X03, 2.54mm_Pin_Headers:Interconnect_1x03, F.Cu at (115.6, 108.0)
- added J24: INTERCONNECT_1X03, 2.54mm_Pin_Headers:Interconnect_1x03, F.Cu at (115.6, 57.1)
- added J24: INTERCONNECT_1X03, 2.54mm_Pin_Headers:Interconnect_1x03, F.Cu at (115.6, 105.4)
- added J25: INTERCONNECT_1X03, 2.54mm_Pin_Headers:Interconnect_1x03, F.Cu at (115.6, 59.7)
- added J25: INTERCONNECT_1X03, 2.54mm_Pin_Headers:Interconnect_1x03, F.Cu at (115.6, 102.9)
- added J26: INTERCONNECT_1X03, 2.54mm_Pin_Headers:Interconnect_1x03, F.Cu at (115.6, 62.2)
- added J26: INTERCONNECT_1X03, 2.54mm_Pin_Headers:Interconnect_1x03, F.Cu at (115.6, 100.3)
- added J27: INTERCONNECT_1X03, 2.54mm_Pin_Headers:Interconnect_1x03, F.Cu at (115.6, 64.8)
- added J27: INTERCONNECT_1X03, 2.54mm_Pin_Headers:Interconnect_1x03, F.Cu at (115.6, 97.8)
- added J28: INTERCONNECT_1X03, 2.54mm_Pin_Headers:Interconnect_1x03, F.Cu at (115.6, 67.3)
- added J28: INTERCONNECT_1X03, 2.54mm_Pin_Headers:Interconnect_1x03, F.Cu at (115.6, 95.2)
- added J29: INTERCONNECT_1X03, 2.54mm_Pin_Headers:Interconnect_1x03, F.Cu at (115.6, 69.8)
- added J29: INTERCONNECT_1X03, 2.54mm_Pin_Headers:Interconnect_1x03, F.Cu at (115.6, 92.7)
- added J3: INTERCONNECT_1X03, 2.54mm_Pin_Headers:Interconnect_1x03, F.Cu at (123.2, 44.5)
- added J3: INTERCONNECT_1X03, 2.54mm_Pin_Headers:Interconnect_1x03, F.Cu at (123.2, 118.1)
- added J30: INTERCONNECT_1X03, 2.54mm_Pin_Headers:Interconnect_1x03, F.Cu at (115.6, 72.4)
- added J30: INTERCONNECT_1X03, 2.54mm_Pin_Headers:Interconnect_1x03, F.Cu at (115.6, 90.2)
- added J31: INTERCONNECT_1X03, 2.54mm_Pin_Headers:Interconnect_1x03, F.Cu at (115.6, 74.9)
- added J31: INTERCONNECT_1X03, 2.54mm_Pin_Headers:Interconnect_1x03, F.Cu at (115.6, 87.6)
- added J32: INTERCONNECT_1X03, 2.54mm_Pin_Headers:Interconnect_1x03, F.Cu at (115.6, 77.5)
- added J32: INTERCONNECT_1X03, 2.54mm_Pin_Headers:Interconnect_1x03, F.Cu at (115.6, 85.1)
- added J33: INTERCONNECT_1X03, 2.54mm_Pin_Headers:Interconnect_1x03, F.Cu at (102.9, 39.4)
- added J33: INTERCONNECT_1X03, 2.54mm_Pin_Headers:Interconnect_1x03, F.Cu at (102.9, 123.2)
- added J34: INTERCONNECT_1X03, 2.54mm_Pin_Headers:Interconnect_1x03, F.Cu at (102.9, 41.9)
- added J34: INTERCONNECT_1X03, 2.54mm_Pin_Headers:Interconnect_1x03, F.Cu at (102.9, 120.7)
- added J35: INTERCONNECT_1X03, 2.54mm_Pin_Headers:Interconnect_1x03, F.Cu at (102.9, 44.5)
- added J35: INTERCONNECT_1X03, 2.54mm_Pin_Headers:Interconnect_1x03, F.Cu at (102.9, 118.1)
- added J36: INTERCONNECT_1X03, 2.54mm_Pin_Headers:Interconnect_1x03, F.Cu at (102.9, 47.0)
- added J36: INTERCONNECT_1X03, 2.54mm_Pin_Headers:Interconnect_1x03, F.Cu at (102.9, 115.6)
- added J37: INTERCONNECT_1X03, 2.54mm_Pin_Headers:Interconnect_1x03, F.Cu at (102.9, 49.5)
- added J37: INTERCONNECT_1X03, 2.54mm_Pin_Headers:Interconnect_1x03, F.Cu at (102.9, 113.0)
- added J38: INTERCONNECT_1X03, 2.54mm_Pin_Headers:Interconnect_1x03, F.Cu at (102.9, 52.1)
- added J38: INTERCONNECT_1X03, 2.54mm_Pin_Headers:Interconnect_1x03, F.Cu at (102.9, 110.5)
- added J39: INTERCONNECT_1X03, 2.54mm_Pin_Headers:Interconnect_1x03, F.Cu at (102.9, 54.6)
- added J39: INTERCONNECT_1X03, 2.54mm_Pin_Headers:Interconnect_1x03, F.Cu at (102.9, 108.0)
- added J4: INTERCONNECT_1X03, 2.54mm_Pin_Headers:Interconnect_1x03, F.Cu at (123.2, 47.0)
- added J4: INTERCONNECT_1X03, 2.54mm_Pin_Headers:Interconnect_1x03, F.Cu at (123.2, 115.6)
- added J40: INTERCONNECT_1X03, 2.54mm_Pin_Headers:Interconnect_1x03, F.Cu at (102.9, 57.1)
- added J40: INTERCONNECT_1X03, 2.54mm_Pin_Headers:Interconnect_1x03, F.Cu at (102.9, 105.4)
- added J41: INTERCONNECT_1X03, 2.54mm_Pin_Headers:Interconnect_1x03, F.Cu at (102.9, 59.7)
- added J41: INTERCONNECT_1X03, 2.54mm_Pin_Headers:Interconnect_1x03, F.Cu at (102.9, 102.9)
- added J42: INTERCONNECT_1X03, 2.54mm_Pin_Headers:Interconnect_1x03, F.Cu at (102.9, 62.2)
- added J42: INTERCONNECT_1X03, 2.54mm_Pin_Headers:Interconnect_1x03, F.Cu at (102.9, 100.3)
- added J43: INTERCONNECT_1X03, 2.54mm_Pin_Headers:Interconnect_1x03, F.Cu at (102.9, 64.8)
- added J43: INTERCONNECT_1X03, 2.54mm_Pin_Headers:Interconnect_1x03, F.Cu at (102.9, 97.8)
- added J44: INTERCONNECT_1X03, 2.54mm_Pin_Headers:Interconnect_1x03, F.Cu at (102.9, 67.3)
- added J44: INTERCONNECT_1X03, 2.54mm_Pin_Headers:Interconnect_1x03, F.Cu at (102.9, 95.2)
- added J45: INTERCONNECT_1X03, 2.54mm_Pin_Headers:Interconnect_1x03, F.Cu at (102.9, 69.8)
- added J45: INTERCONNECT_1X03, 2.54mm_Pin_Headers:Interconnect_1x03, F.Cu at (102.9, 92.7)
- added J46: INTERCONNECT_1X03, 2.54mm_Pin_Headers:Interconnect_1x03, F.Cu at (102.9, 72.4)
- added J46: INTERCONNECT_1X03, 2.54mm_Pin_Headers:Interconnect_1x03, F.Cu at (102.9, 90.2)
- added J47: INTERCONNECT_1X03, 2.54mm_Pin_Headers:Interconnect_1x03, F.Cu at (102.9, 74.9)
- added J47: INTERCONNECT_1X03, 2.54mm_Pin_Headers:Interconnect_1x03, F.Cu at (102.9, 87.6)
- added J48: INTERCONNECT_1X03, 2.54mm_Pin_Headers:Interconnect_1x03, F.Cu at (102.9, 77.5)
- added J48: INTERCONNECT_1X03, 2.54mm_Pin_Headers:Interconnect_1x03, F.Cu at (102.9, 85.1)
- added J49: INTERCONNECT_1X03, 2.54mm_Pin_Headers:Interconnect_1x03, F.Cu at (95.2, 39.4)
- added J49: INTERCONNECT_1X03, 2.54mm_Pin_Headers:Interconnect_1x03, F.Cu at (95.2, 123.2)
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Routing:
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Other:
- outline, holes or cut-outs redrawn
